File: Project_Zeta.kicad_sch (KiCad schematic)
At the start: 14 parts, among them J1 Conn_01x20, J2 Conn_01x20, J3 Screw_Terminal_01x02, J4 Screw_Terminal_01x04, J5 Screw_Terminal_01x04, J6 Screw_Terminal_01x04, J7 Screw_Terminal_01x04, J8 Conn_01x03, J9 Conn_01x03

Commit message: Init with Rev 1.1
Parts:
- removed J8, J9: Conn_01x03, Connector_PinHeader_2.54mm:PinHeader_1x03_P2.54mm_Vertical, symbol Connector_Generic:Conn_01x03
- added C3: 0.1uF, symbol Device:C
- added C4: 100uF, symbol Device:C_Polarized
- added D3: SS14, Diode_SMD:D_SMA, symbol Diode:SS14
- added D4: SMAJ5.0A, Diode_SMD:D_SMA, symbol Diode:SMAJ5.0A
- added F2: Polyfuse, symbol Device:Polyfuse
- added J4: Conn_01x08, Connector_PinHeader_2.54mm:PinHeader_1x08_P2.54mm_Horizontal, symbol Connector_Generic:Conn_01x08
- added J5: Conn_01x02, Connector_PinHeader_2.54mm:PinHeader_1x02_P2.54mm_Horizontal, symbol Connector_Generic:Conn_01x02
- added J6, J7: Conn_01x01, Connector_Wire:SolderWire-0.25sqmm_1x01_D0.65mm_OD2mm, symbol Connector_Generic:Conn_01x01
- added RESET1: Conn_01x02_Pin, Connector_PinHeader_2.54mm:PinHeader_1x02_P2.54mm_Vertical, symbol Connector:Conn_01x02_Pin
- H1: renamed from J4; value Screw_Terminal_01x04 -> TerminalBlock_Phoenix_MKDS-1,5-4_1x04_P5.00mm_Horizontal; footprint (none) -> TerminalBlock_Phoenix_MKDS-1,5-4_1x04_P5.00mm_Horizontal
- H2: renamed from J5; value Screw_Terminal_01x04 -> TerminalBlock_Phoenix_MKDS-1,5-4_1x04_P5.00mm_Horizontal; footprint (none) -> TerminalBlock_Phoenix_MKDS-1,5-4_1x04_P5.00mm_Horizontal
- H3: renamed from J7; value Screw_Terminal_01x04 -> TerminalBlock_Phoenix_MKDS-1,5-4_1x04_P5.00mm_Horizontal; footprint (none) -> TerminalBlock_Phoenix_MKDS-1,5-4_1x04_P5.00mm_Horizontal
- H4: renamed from J6; value Screw_Terminal_01x04 -> TerminalBlock_Phoenix_MKDS-1,5-4_1x04_P5.08mm_Horizontal; footprint (none) -> TerminalBlock_Phoenix_MKDS-1,5-4_1x04_P5.00mm_Horizontal
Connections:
- net 3V3_OUT: now also H1.2 (Pin_2), H2.2 (Pin_2), H3.2 (Pin_2), H4.2 (Pin_2), J4.7 (Pin_7)
- net GND: now also F2.2, J4.8 (Pin_8), J6.1 (Pin_1), J7.1 (Pin_1), RESET1.1 (Pin_1)
- net GP0: now also J2.20 (Pin_20); no longer J2.1 (Pin_1)
- net GP1: now also J2.19 (Pin_19); no longer J2.2 (Pin_2)
- net GP10: now also J2.7 (Pin_7), J4.4 (Pin_4); no longer J2.14 (Pin_14)
- net GP11: now also J2.6 (Pin_6), J4.3 (Pin_3); no longer J2.15 (Pin_15)
- net GP12: now also J2.5 (Pin_5), J4.2 (Pin_2); no longer J2.16 (Pin_16)
- net GP13: now also J2.4 (Pin_4), J4.1 (Pin_1); no longer J2.17 (Pin_17)
- net GP14: now also J2.2 (Pin_2); no longer J2.19 (Pin_19)
- net GP15: now also J2.1 (Pin_1); no longer J2.20 (Pin_20)
- net GP16: now also H3.3 (Pin_3)
- net GP17: now also H3.4 (Pin_4)
- net GP18: now also H2.3 (Pin_3)
- net GP19: now also H2.4 (Pin_4)
- net GP2: now also J2.17 (Pin_17); no longer J2.4 (Pin_4)
- net GP20: now also H1.3 (Pin_3)
- net GP21: now also H1.4 (Pin_4)
- net GP22: no longer J1.9 (GP22)
- net GP26: now also H4.3 (Pin_3)
- net GP27: now also H4.4 (Pin_4)
- net GP3: now also J2.16 (Pin_16); no longer J2.5 (Pin_5)
- net GP4: now also J2.15 (Pin_15); no longer J2.6 (Pin_6)
- net GP5: now also J2.14 (Pin_14); no longer J2.7 (Pin_7)
- net GP6: now also J2.12 (Pin_12); no longer J2.9 (Pin_9)
- net GP7: now also J2.11 (Pin_11); no longer J2.10 (Pin_10)
- net GP8: now also J2.10 (Pin_10), J4.6 (Pin_6); no longer J2.11 (Pin_11)
- net GP9: now also J2.9 (Pin_9), J4.5 (Pin_5); no longer J2.12 (Pin_12)
- net RUN: now also RESET1.2 (Pin_2)
- new net: C3.1, C4.1, D3.1 (K), D4.1 (A1)
- new net: C3.2, C4.2
- new net: D3.2 (A), F2.1
- new net 3V3_EXT: J5.1 (Pin_1), J5.2 (Pin_2)
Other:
- title: (none) -> Project Zeta
- moved on the sheet: H2, J2

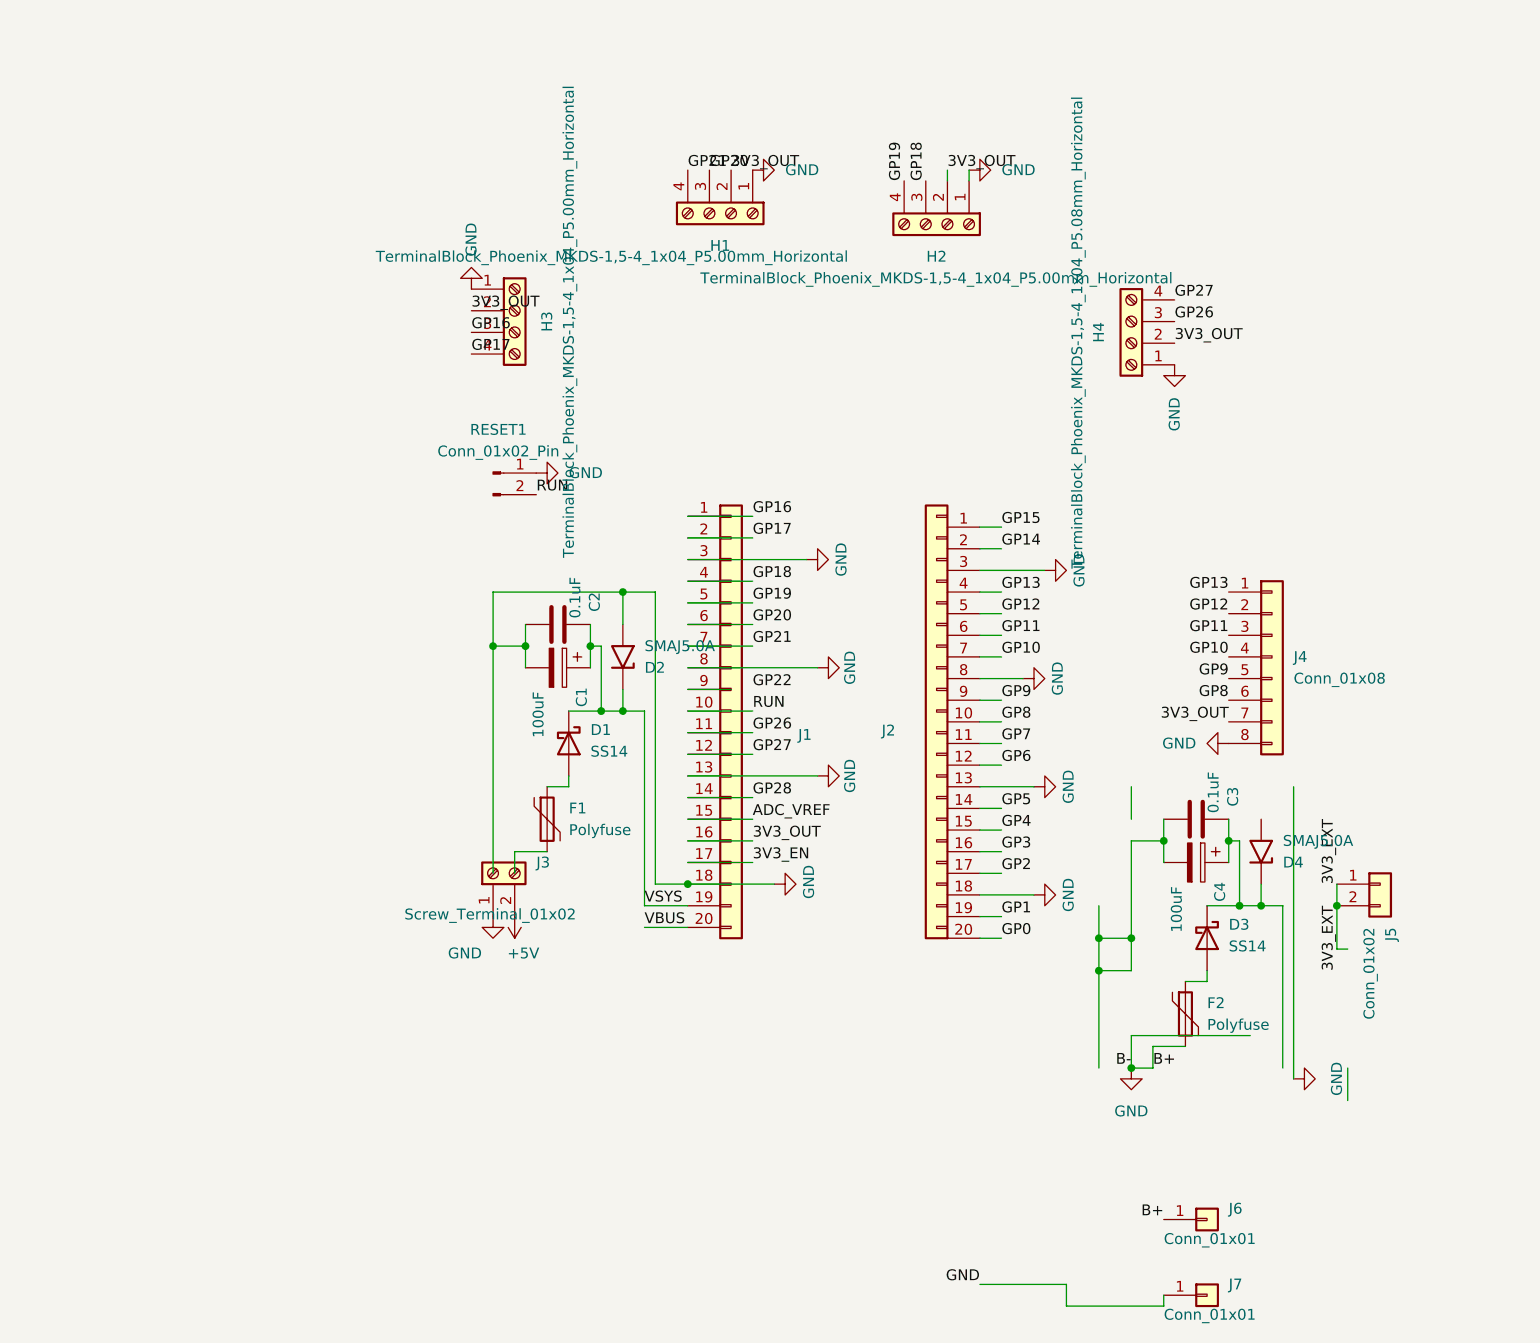
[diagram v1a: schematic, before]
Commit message: Updated some nets and added via for some GND point
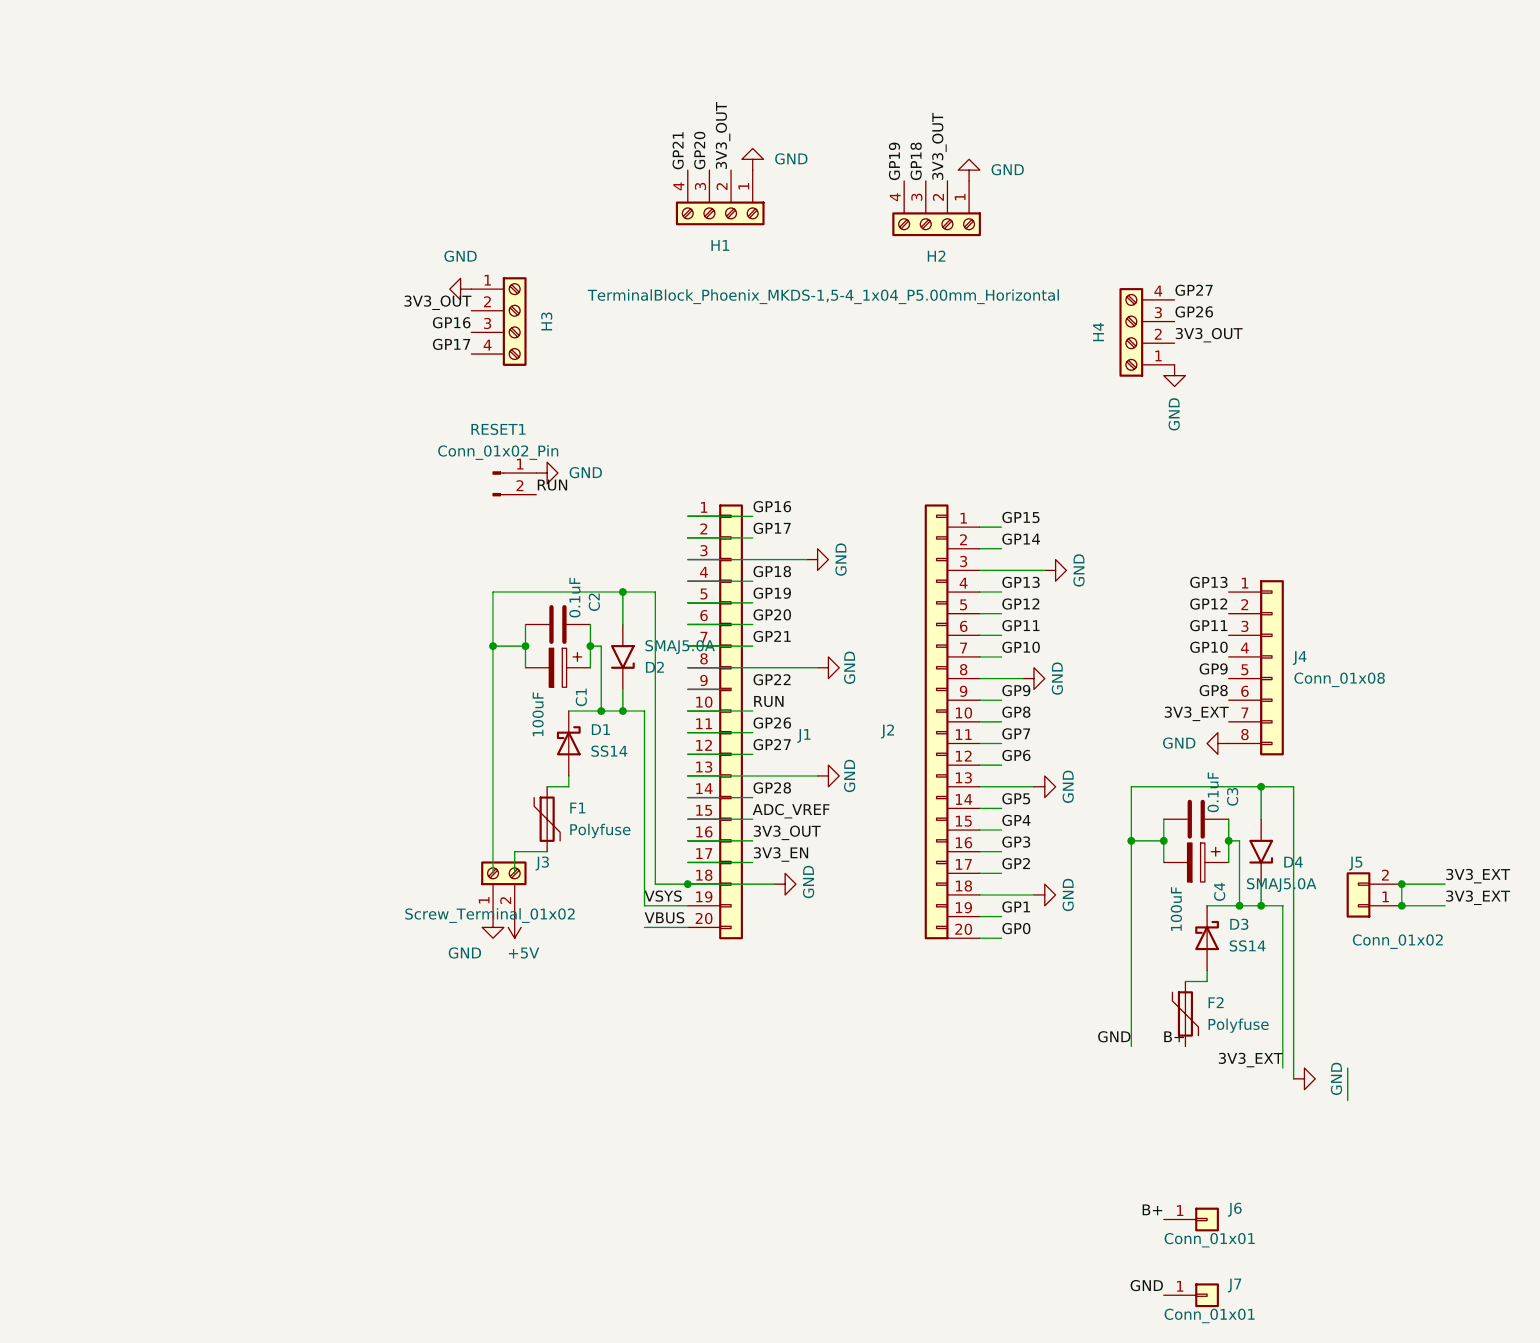
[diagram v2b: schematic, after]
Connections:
- net 3V3_EXT: now also C3.1, C4.1, D3.1 (K), D4.1 (A1), J4.7 (Pin_7)
- net 3V3_OUT: no longer J4.7 (Pin_7)
- net GND: now also C3.2, C4.2, D4.2 (A2); no longer F2.2, J6.1 (Pin_1)
- new net B+: F2.2, J6.1 (Pin_1)
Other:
- moved on the sheet: J5

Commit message: Updated something IDK I forgotten
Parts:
- C1, C4: footprint (none) -> Capacitor_THT:CP_Radial_D6.3mm_P2.50mm
- C2, C3: footprint (none) -> Capacitor_THT:C_Disc_D5.0mm_W2.5mm_P2.50mm
- F1, F2: footprint (none) -> Fuse:Fuse_Bourns_MF-RHT050
- J3: footprint (none) -> TerminalBlock_Phoenix:TerminalBlock_Phoenix_MKDS-1,5-2_1x02_P5.00mm_Horizontal
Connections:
- net +5V: now also F1.1
- net at D1.2 (A): now also F1.2; no longer F1.1
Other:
- moved on the sheet: F1
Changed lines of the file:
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@@
 	(wire
 		(pts
-			(xy 119.38 105.41) (xy 119.38 107.95)
-		)
-		(stroke
-			(width 0)
-			(type default)
-		)
-	)
-	(wire
-		(pts
 			(xy 132.08 74.93) (xy 132.08 78.74)
 		)
@@
 	(wire
 		(pts
-			(xy 123.19 97.79) (xy 125.73 97.79)
-		)
-		(stroke
-			(width 0)
-			(type default)
-		)
-	)
-	(wire
-		(pts
 			(xy 217.17 134.62) (xy 217.17 130.81)
 		)
@@
 	(wire
 		(pts
-			(xy 123.19 105.41) (xy 119.38 105.41)
-		)
-		(stroke
-			(width 0)
-			(type default)
-		)
-	)
-	(wire
-		(pts
 			(xy 147.32 73.66) (xy 139.7 73.66)
 		)
@@
 		)
 	)
+	(label "+5V"
+		(at 125.73 105.41 0)
+		(effects
+			(font
+				(size 1.27 1.27)
+			)
+			(justify left bottom)
+		)
+	)
 	(label "VBUS"
 		(at 134.62 114.3 0)
@@
 			)
 		)
-		(property "Footprint" ""
+		(property "Footprint" "Capacitor_THT:C_Disc_D5.0mm_W2.5mm_P2.50mm"
 			(at 195.58 102.5652 0)
 			(hide yes)
@@
 	(symbol
 		(lib_id "Device:Polyfuse")
-		(at 123.19 101.6 0)
+		(at 125.73 101.6 180)
 		(unit 1)
 		(body_style 1)
@@
 		(fields_autoplaced yes)
 		(property "Reference" "F1"
-			(at 125.73 100.3299 0)
+			(at 128.27 100.3299 0)
 			(show_name no)
 			(do_not_autoplace no)
@@
 					(size 1.27 1.27)
 				)
-				(justify left)
+				(justify right)
 			)
 		)
 		(property "Value" "Polyfuse"
-			(at 125.73 102.8699 0)
+			(at 128.27 102.8699 0)
 			(show_name no)
 			(do_not_autoplace no)
@@
 					(size 1.27 1.27)
 				)
-				(justify left)
+				(justify right)
 			)
 		)
-		(property "Footprint" ""
-			(at 124.46 106.68 0)
+		(property "Footprint" "Fuse:Fuse_Bourns_MF-RHT050"
+			(at 124.46 96.52 0)
 			(hide yes)
 			(show_name no)
@@
 		)
 		(property "Datasheet" ""
-			(at 123.19 101.6 0)
+			(at 125.73 101.6 0)
 			(hide yes)
 			(show_name no)
@@
 		)
 		(property "Description" "Resettable fuse, polymeric positive temperature coefficient"
-			(at 123.19 101.6 0)
+			(at 125.73 101.6 0)
 			(hide yes)
 			(show_name no)
@@
 			)
 		)
-		(property "Footprint" ""
+		(property "Footprint" "Capacitor_THT:CP_Radial_D6.3mm_P2.50mm"
 			(at 195.58 107.6452 0)
 			(hide yes)
@@
 			)
 		)
-		(property "Footprint" ""
+		(property "Footprint" "Capacitor_THT:C_Disc_D5.0mm_W2.5mm_P2.50mm"
 			(at 120.65 79.7052 0)
 			(hide yes)
@@
 			)
 		)
-		(property "Footprint" ""
+		(property "Footprint" "Fuse:Fuse_Bourns_MF-RHT050"
 			(at 199.39 129.54 0)
 			(hide yes)
@@
 			)
 		)
-		(property "Footprint" ""
+		(property "Footprint" "Capacitor_THT:CP_Radial_D6.3mm_P2.50mm"
 			(at 120.65 84.7852 0)
 			(hide yes)
@@
 			)
 		)
-		(property "Footprint" ""
+		(property "Footprint" "TerminalBlock_Phoenix:TerminalBlock_Phoenix_MKDS-1,5-2_1x02_P5.00mm_Horizontal"
 			(at 116.84 107.95 0)
 			(hide yes)

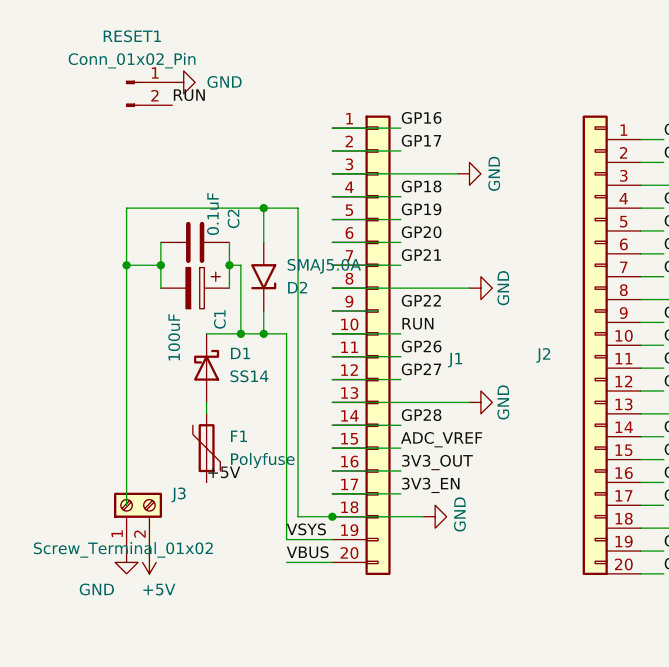
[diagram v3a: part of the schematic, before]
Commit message: Fix wrong direction Diode
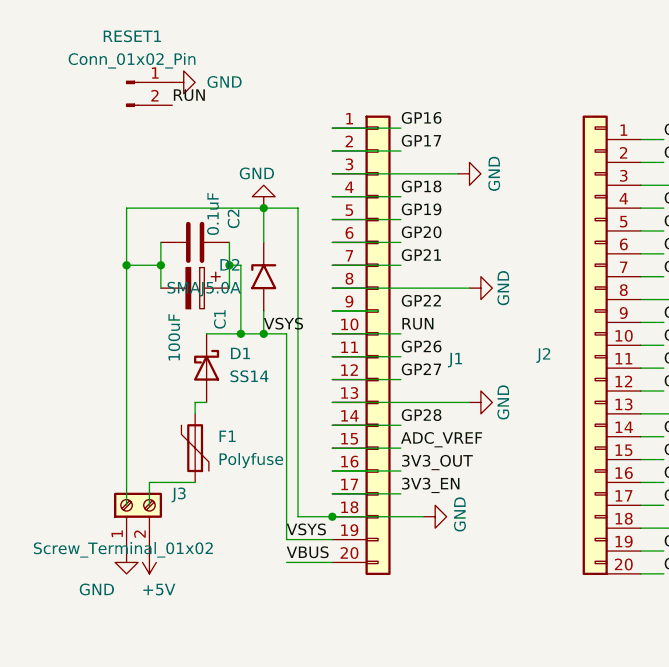
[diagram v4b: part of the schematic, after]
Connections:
- net +5V: no longer F1.1
- net GND: now also D2.1 (A1); no longer D2.2 (A2)
- net VSYS: now also D2.2 (A2); no longer D2.1 (A1)
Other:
- moved on the sheet: D2, F1

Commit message: Fix some schematic and add Gas Discharge Tube from GND to Earth
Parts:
- added GD1: GDT_2Pin, Resistor_THT:R_Axial_DIN0411_L9.9mm_D3.6mm_P15.24mm_Horizontal, symbol Device:GDT_2Pin
- added J8: Screw_Terminal_01x02, TerminalBlock_Phoenix:TerminalBlock_Phoenix_MKDS-1,5-2_1x02_P5.00mm_Horizontal, symbol Connector:Screw_Terminal_01x02
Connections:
- net +5V: now also F1.1
- net GND: now also D2.2 (A2), GD1.1; no longer D2.1 (A1)
- net VSYS: now also D2.1 (A1); no longer D2.2 (A2)
- new net Earth_Clean: GD1.2, J8.1 (Pin_1), J8.2 (Pin_2)
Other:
- moved on the sheet: D2, F1, J3, J6, J7
